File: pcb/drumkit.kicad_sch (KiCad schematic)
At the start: 22 parts, among them IC1 ULN2065B, J1 BATTERY, J2 Conn_01x04_Female, J3 CH1, J4 CH2, J5 CH3, SW1 BUTTON1, SW2 BUTTON2, SW3 BUTTON3, SW4 BUTTON4, SW5 POWER_SW, U1 Pico, U2 Mini360

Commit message: fix board
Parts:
- removed IC1: ULN2065B, Package_DIP:DIP-16_W7.62mm_LongPads, symbol ULN2065B:ULN2065B
- removed J3: CH1, TerminalBlock:TerminalBlock_bornier-2_P5.08mm, symbol Connector:Screw_Terminal_01x02
- removed J4: CH2, TerminalBlock:TerminalBlock_bornier-2_P5.08mm, symbol Connector:Screw_Terminal_01x02
- removed J5: CH3, TerminalBlock:TerminalBlock_bornier-2_P5.08mm, symbol Connector:Screw_Terminal_01x02
- removed U2: Mini360, Mini360_step-down:Mini360_step-down, symbol mini360:Mini360
- added U2: ~, chinese_modules:charger, symbol chinese_modules:charger
- added U3, U5, U7: ~, chinese_modules:dc-dc module, symbol chinese_modules:dc-dc
- added U4, U6, U8: ~, chinese_modules:xy-mos, symbol chinese_modules:xy-mos
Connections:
- net +BATT: now also U1.39 (VSYS), U3.2 (Vin+), U5.2 (Vin+), U7.2 (Vin+)
- net GND: now also U1.23 (GND), U2.4 (B-), U3.1 (Vin+), U3.3 (Out-), U4.2 (Vin-), U5.1 (Vin+), U7.1 (Vin+); no longer J2.1 (Pin_1), U1.42 (GND)
- net at U1.15 (GPIO11): now also D2.2 (A); no longer S1.1
- net at U1.12 (GPIO9): now also SW2.2; no longer S1.A (CH_A)
- net at S1.B (CH_B): now also U1.24 (GPIO18); no longer U1.14 (GPIO10)
- net at D3.2 (A): now also U1.17 (GPIO13); no longer U1.19 (GPIO14)
- net at J1.1 (Pin_1), SW5.1 (A): now also U2.3 (B+)
- net at SW1.2: now also U1.11 (GPIO8); no longer U1.7 (GPIO5)
- net at U1.9 (GPIO6): no longer SW2.2
- net at SW3.2: now also U1.16 (GPIO12); no longer U1.10 (GPIO7)
- net at SW4.2: now also U1.19 (GPIO14); no longer U1.11 (GPIO8)
- net at U1.13 (GND): now also J2.1 (Pin_1)
- net at D1.2 (A): now also U1.14 (GPIO10); no longer U1.16 (GPIO12)
- net at U1.21 (GPIO16): now also S1.1
- net at U1.22 (GPIO17): now also S1.A (CH_A)
- net at U1.29 (GPIO22): now also U8.6 (trig)
- net at U1.31 (GPIO26_ADC0): now also U6.6 (trig)
- net at U1.32 (GPIO27_ADC1): now also U4.6 (trig)
- new net: U7.4 (Out+), U8.1 (Vin+)
- new net: U7.3 (Out-), U8.2 (Vin-)
- new net: U5.3 (Out-), U6.2 (Vin-)
- new net: U5.4 (Out+), U6.1 (Vin+)
- new net: U3.4 (Out+), U4.1 (Vin+)

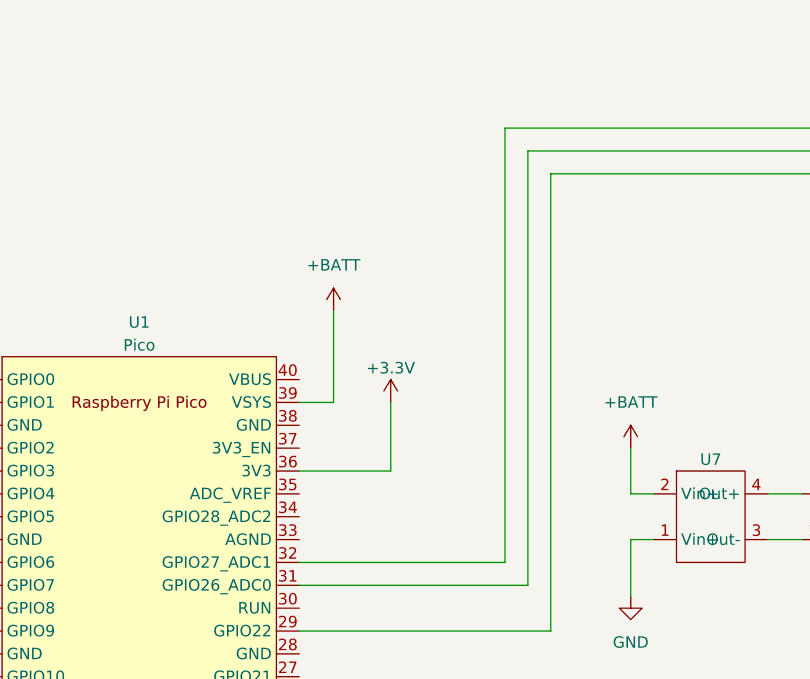
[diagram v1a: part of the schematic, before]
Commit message: add voltage divider
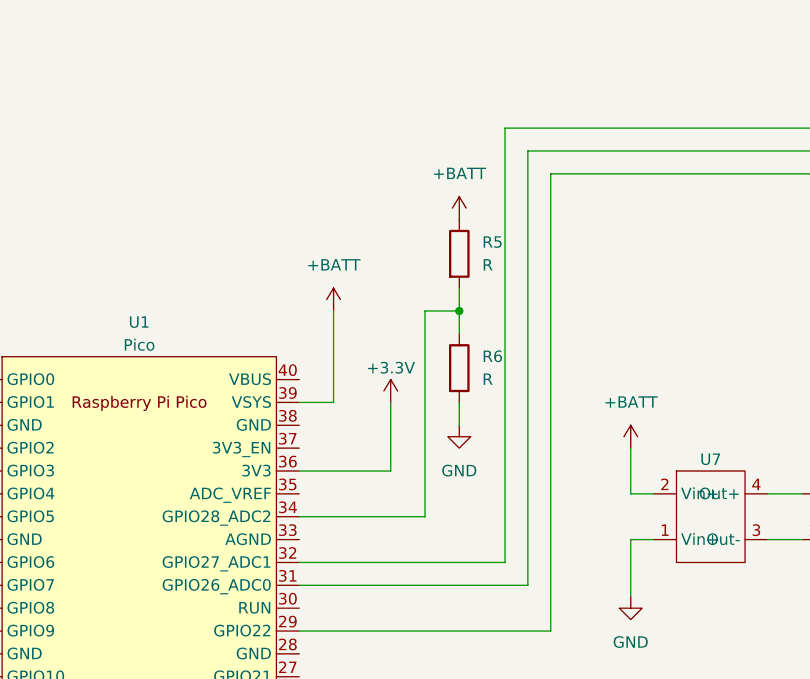
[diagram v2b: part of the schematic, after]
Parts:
- added R5, R6: R, Resistor_THT:R_Axial_DIN0309_L9.0mm_D3.2mm_P12.70mm_Horizontal, symbol Device:R
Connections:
- net +BATT: now also R5.1
- net GND: now also R6.2
- net at U1.34 (GPIO28_ADC2): now also R5.2, R6.1
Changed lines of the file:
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@@
   (junction (at 27.94 138.43) (diameter 0) (color 0 0 0 0)
   )
+  (junction (at 143.51 58.42) (diameter 0) (color 0 0 0 0)
+  )
   (junction (at 27.94 127) (diameter 0) (color 0 0 0 0)
   )
@@
     (stroke (width 0) (type default))
   )
+  (wire (pts (xy 139.7 81.28) (xy 139.7 58.42))
+    (stroke (width 0) (type default))
+  )
   (wire (pts (xy 157.48 124.46) (xy 160.02 124.46))
     (stroke (width 0) (type default))
@@
     (stroke (width 0) (type default))
   )
+  (wire (pts (xy 125.73 81.28) (xy 139.7 81.28))
+    (stroke (width 0) (type default))
+  )
   (wire (pts (xy 62.23 168.91) (xy 62.23 172.72))
     (stroke (width 0) (type default))
@@
     (stroke (width 0) (type default))
   )
+  (wire (pts (xy 143.51 58.42) (xy 143.51 60.96))
+    (stroke (width 0) (type default))
+  )
   (wire (pts (xy 67.31 111.76) (xy 90.17 111.76))
     (stroke (width 0) (type default))
@@
     (stroke (width 0) (type default))
   )
+  (wire (pts (xy 143.51 55.88) (xy 143.51 58.42))
+    (stroke (width 0) (type default))
+  )
   (wire (pts (xy 52.07 161.29) (xy 52.07 149.86))
     (stroke (width 0) (type default))
@@
     (stroke (width 0) (type default))
   )
+  (wire (pts (xy 139.7 58.42) (xy 143.51 58.42))
+    (stroke (width 0) (type default))
+  )
   (wire (pts (xy 90.17 114.3) (xy 82.55 114.3))
     (stroke (width 0) (type default))
@@
   )
   (wire (pts (xy 162.56 111.76) (xy 125.73 111.76))
+    (stroke (width 0) (type default))
+  )
+  (wire (pts (xy 143.51 68.58) (xy 143.51 71.12))
     (stroke (width 0) (type default))
   )
@@
         (path "/13d14c25-8baa-4714-9b30-86acf6c3cb37"
           (reference "SW5") (unit 1)
+        )
+      )
+    )
+  )
+  (symbol (lib_name "R_1") (lib_id "Device:R") (at 143.51 64.77 0) (unit 1)
+    (in_bom yes) (on_board yes) (dnp no) (fields_autoplaced)
+    (property "Reference" "R6" (at 146.05 63.5 0)
+      (effects (font (size 1.27 1.27)) (justify left))
+    )
+    (property "Value" "R" (at 146.05 66.04 0)
+      (effects (font (size 1.27 1.27)) (justify left))
+    )
+    (property "Footprint" "Resistor_THT:R_Axial_DIN0309_L9.0mm_D3.2mm_P12.70mm_Horizontal" (at 141.732 64.77 90)
+      (effects (font (size 1.27 1.27)) hide)
+    )
+    (property "Datasheet" "~" (at 143.51 64.77 0)
+      (effects (font (size 1.27 1.27)) hide)
+    )
+    (pin "1")
+    (pin "2")
+    (instances
+      (project "drumkit"
+        (path "/13d14c25-8baa-4714-9b30-86acf6c3cb37"
+          (reference "R6") (unit 1)
         )
       )
@@
     )
   )
+  (symbol (lib_id "power:GND") (at 143.51 71.12 0) (unit 1)
+    (in_bom yes) (on_board yes) (dnp no)
+    (property "Reference" "#PWR011" (at 143.51 77.47 0)
+      (effects (font (size 1.27 1.27)) hide)
+    )
+    (property "Value" "GND" (at 143.51 76.2 0)
+      (effects (font (size 1.27 1.27)))
+    )
+    (property "Footprint" "" (at 143.51 71.12 0)
+      (effects (font (size 1.27 1.27)) hide)
+    )
+    (property "Datasheet" "" (at 143.51 71.12 0)
+      (effects (font (size 1.27 1.27)) hide)
+    )
+    (pin "1")
+    (instances
+      (project "drumkit"
+        (path "/13d14c25-8baa-4714-9b30-86acf6c3cb37"
+          (reference "#PWR011") (unit 1)
+        )
+      )
+    )
+  )
+  (symbol (lib_id "power:+BATT") (at 143.51 48.26 0) (unit 1)
+    (in_bom yes) (on_board yes) (dnp no)
+    (property "Reference" "#PWR05" (at 143.51 52.07 0)
+      (effects (font (size 1.27 1.27)) hide)
+    )
+    (property "Value" "+BATT" (at 143.51 43.18 0)
+      (effects (font (size 1.27 1.27)))
+    )
+    (property "Footprint" "" (at 143.51 48.26 0)
+      (effects (font (size 1.27 1.27)) hide)
+    )
+    (property "Datasheet" "" (at 143.51 48.26 0)
+      (effects (font (size 1.27 1.27)) hide)
+    )
+    (pin "1")
+    (instances
+      (project "drumkit"
+        (path "/13d14c25-8baa-4714-9b30-86acf6c3cb37"
+          (reference "#PWR05") (unit 1)
+        )
+      )
+    )
+  )
   (symbol (lib_id "Device:LED") (at 82.55 165.1 90) (unit 1)
     (in_bom yes) (on_board yes) (dnp no) (fields_autoplaced)
@@
         )
       )
+    )
+  )
+  (symbol (lib_name "R_1") (lib_id "Device:R") (at 143.51 52.07 0) (unit 1)
+    (in_bom yes) (on_board yes) (dnp no) (fields_autoplaced)
+    (property "Reference" "R5" (at 146.05 50.8 0)
+      (effects (font (size 1.27 1.27)) (justify left))
+    )
+    (property "Value" "R" (at 146.05 53.34 0)
+      (effects (font (size 1.27 1.27)) (justify left))
+    )
+    (property "Footprint" "Resistor_THT:R_Axial_DIN0309_L9.0mm_D3.2mm_P12.70mm_Horizontal" (at 141.732 52.07 90)
+      (effects (font (size 1.27 1.27)) hide)
+    )
+    (property "Datasheet" "~" (at 143.51 52.07 0)
+      (effects (font (size 1.27 1.27)) hide)
+    )
+    (pin "1")
+    (pin "2")
+    (instances
+      (project "drumkit"
+        (path "/13d14c25-8baa-4714-9b30-86acf6c3cb37"
+          (reference "R5") (unit 1)
+        )
+      )

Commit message: cleanup pcb
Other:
- title: (none) -> Drumkit
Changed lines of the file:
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@@
 (kicad_sch (version 20230121) (generator eeschema)
   (paper "A4")
+  (title_block
+    (title "Drumkit")
+    (date "2024-03-25")
+    (rev "1")
+  )
   (junction (at 247.65 82.55) (diameter 0) (color 0 0 0 0)
   )
@@
     (stroke (width 0) (type default))
   )
-  (wire (pts (xy 54.61 38.1) (xy 54.61 78.74))
-    (stroke (width 0) (type default))
-  )
   (wire (pts (xy 30.48 127) (xy 27.94 127))
     (stroke (width 0) (type default))
@@
     (stroke (width 0) (type default))
   )
-  (wire (pts (xy 57.15 76.2) (xy 57.15 40.64))
-    (stroke (width 0) (type default))
-  )
   (wire (pts (xy 81.28 68.58) (xy 90.17 68.58))
     (stroke (width 0) (type default))
@@
     (stroke (width 0) (type default))
   )
-  (wire (pts (xy 59.69 73.66) (xy 59.69 43.18))
-    (stroke (width 0) (type default))
-  )

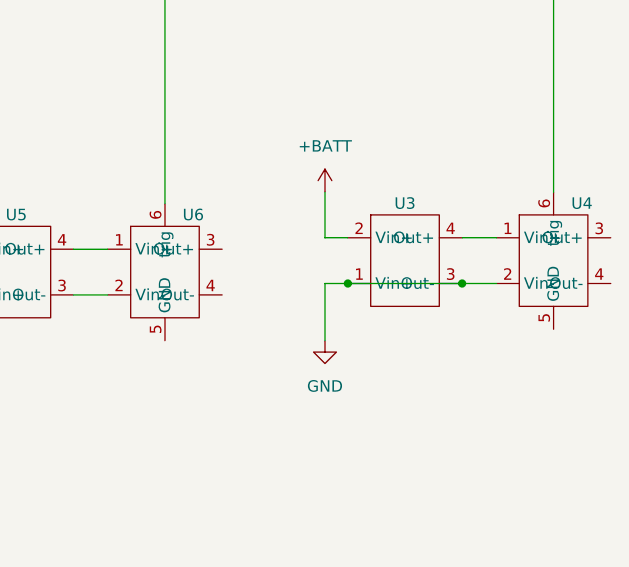
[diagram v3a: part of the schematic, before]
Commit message: cleanup strange connection in schematic and pcb
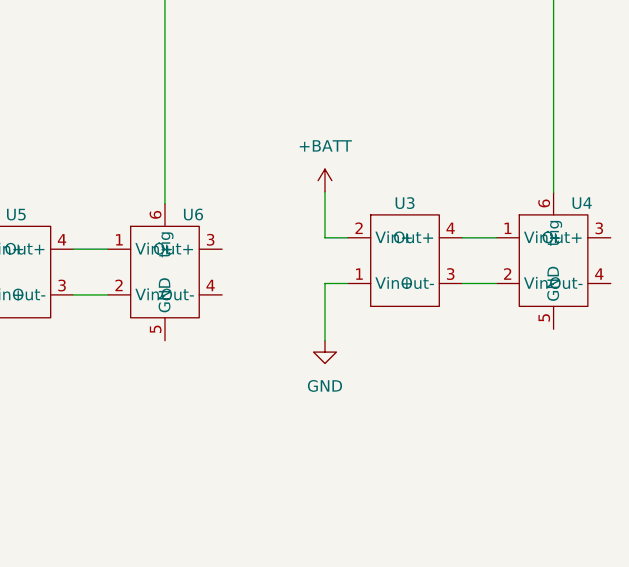
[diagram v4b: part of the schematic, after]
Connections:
- net GND: no longer U3.3 (Out-), U4.2 (Vin-)
- new net: U3.3 (Out-), U4.2 (Vin-)
